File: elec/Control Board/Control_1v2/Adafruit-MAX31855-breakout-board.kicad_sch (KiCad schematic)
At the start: 6 parts

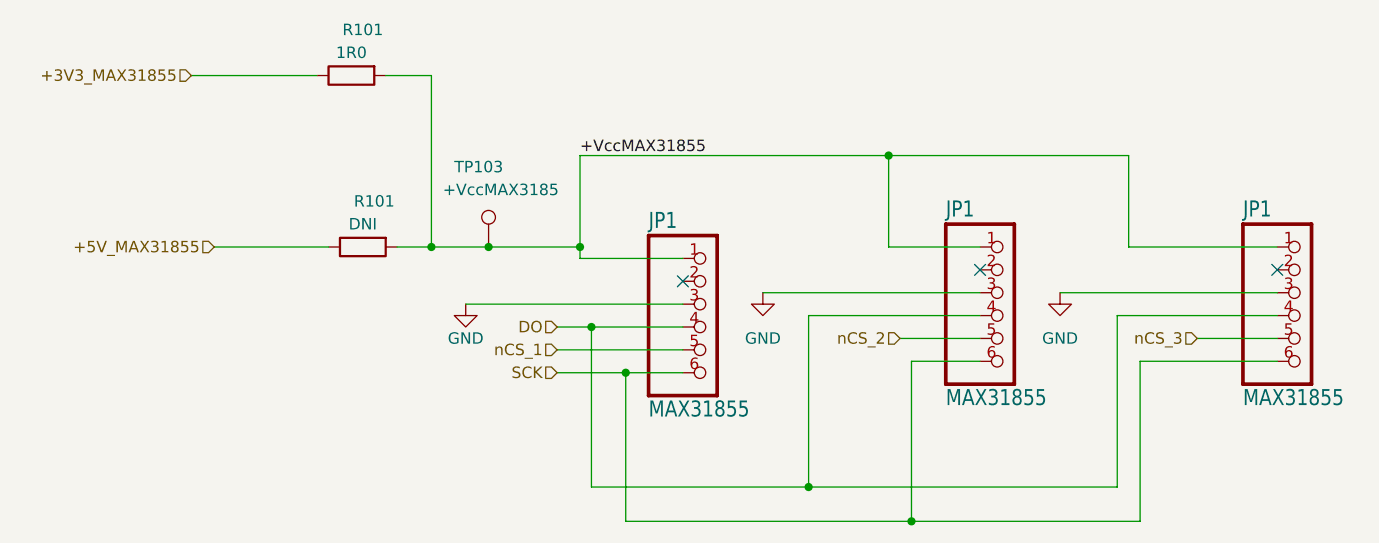
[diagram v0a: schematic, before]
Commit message: PCB V1.2. Add 3d model for power supply footprint. Set many headers connectors for DNI on schematic and PCB.
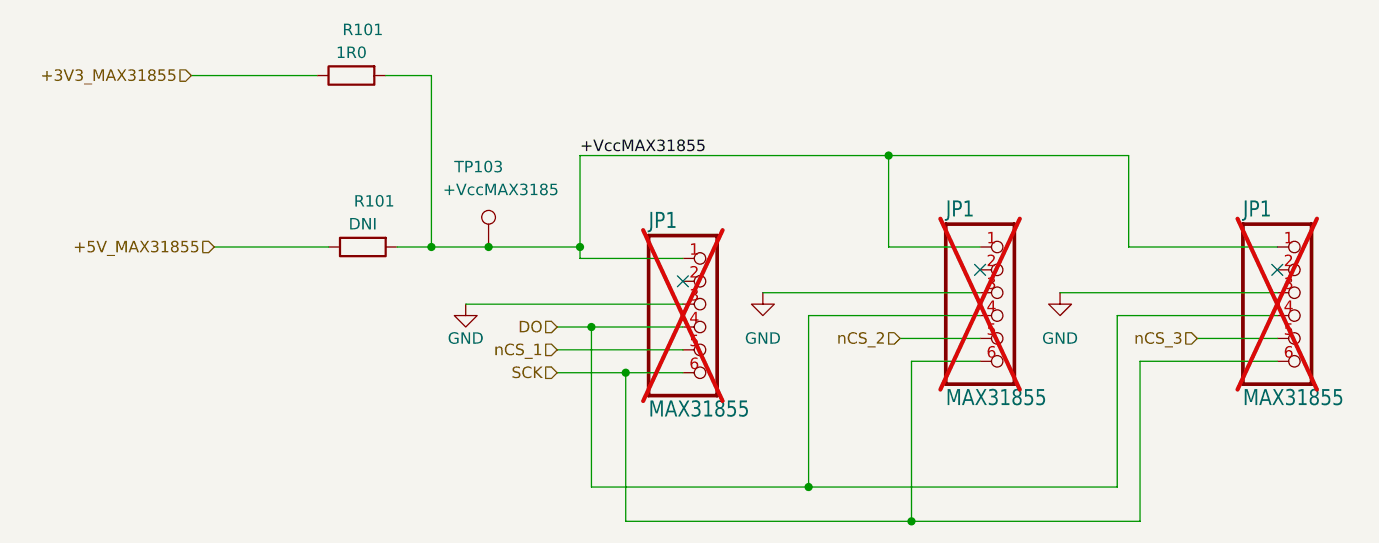
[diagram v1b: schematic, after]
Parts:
- JP1: now not fitted; now left out of the parts list
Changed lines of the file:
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@@
   )
   (symbol (lib_id "Control v1-eagle-import:HEADER-1X676MIL") (at 170.18 110.49 0) (unit 1)
-    (in_bom yes) (on_board yes) (dnp no)
+    (in_bom no) (on_board yes) (dnp yes)
     (property "Reference" "JP1" (at 163.83 99.695 0)
       (effects (font (size 1.778 1.5113)) (justify left bottom))
@@
   )
   (symbol (lib_id "Control v1-eagle-import:HEADER-1X676MIL") (at 137.16 110.49 0) (unit 1)
-    (in_bom yes) (on_board yes) (dnp no)
+    (in_bom no) (on_board yes) (dnp yes)
     (property "Reference" "JP1" (at 130.81 99.695 0)
       (effects (font (size 1.778 1.5113)) (justify left bottom))
@@
   )
   (symbol (lib_id "Control v1-eagle-import:HEADER-1X676MIL") (at 104.14 111.76 0) (unit 1)
-    (in_bom yes) (on_board yes) (dnp no)
+    (in_bom no) (on_board yes) (dnp yes)
     (property "Reference" "JP1" (at 97.79 100.965 0)
       (effects (font (size 1.778 1.5113)) (justify left bottom))

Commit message: PCB V1.2. Add test points of many colors.
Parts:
- TP103: Cost NA -> 0.0696; Distributor 1 (none) -> JLCPCB; Distributor 1 PN (none) -> C5277086; MPN (none) -> RH-5000; Manufacturer (none) -> ronghe
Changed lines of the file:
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@@
       (effects (font (size 1.27 1.27)) hide)
     )
-    (property "Cost" "NA" (at 80.01 102.87 0)
+    (property "Cost" "0.0696" (at 80.01 102.87 0)
       (effects (font (size 1.27 1.27)) hide)
     )
+    (property "Description" "Test Points/Test Rings ROHS red" (at 80.01 102.87 0)
+      (effects (font (size 1.27 1.27)) hide)
+    )
+    (property "Distributor 1 PN" "C5277086" (at 80.01 102.87 0)
+      (effects (font (size 1.27 1.27)) hide)
+    )
+    (property "Distributor 1" "JLCPCB" (at 80.01 102.87 0)
+      (effects (font (size 1.27 1.27)) hide)
+    )
+    (property "MPN" "RH-5000 " (at 80.01 102.87 0)
+      (effects (font (size 1.27 1.27)) hide)
+    )
+    (property "Manufacturer" "ronghe " (at 80.01 102.87 0)
+      (effects (font (size 1.27 1.27)) hide)
+    )
